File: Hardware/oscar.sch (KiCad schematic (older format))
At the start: 49 parts, among them J1 SWD_Header, J2 ChannelA_In, J3 ChannelB_In, J4 ChannelC_In, J5 ChA_Buff_Out, J6 ChB_Buff_Out, J7 ChC_Buff_Out, J8 MIDI_In, J9 Eurorack_16_pin_power, SW1 Left_Encoder, SW2 Right_Encoder, SW3 SW_Push, U1 STM32F446RETx, U2 ILI9341_SPI, U3 MCP6004, U4 TL074, U5 LM1117-3.3, Y1 Crystal

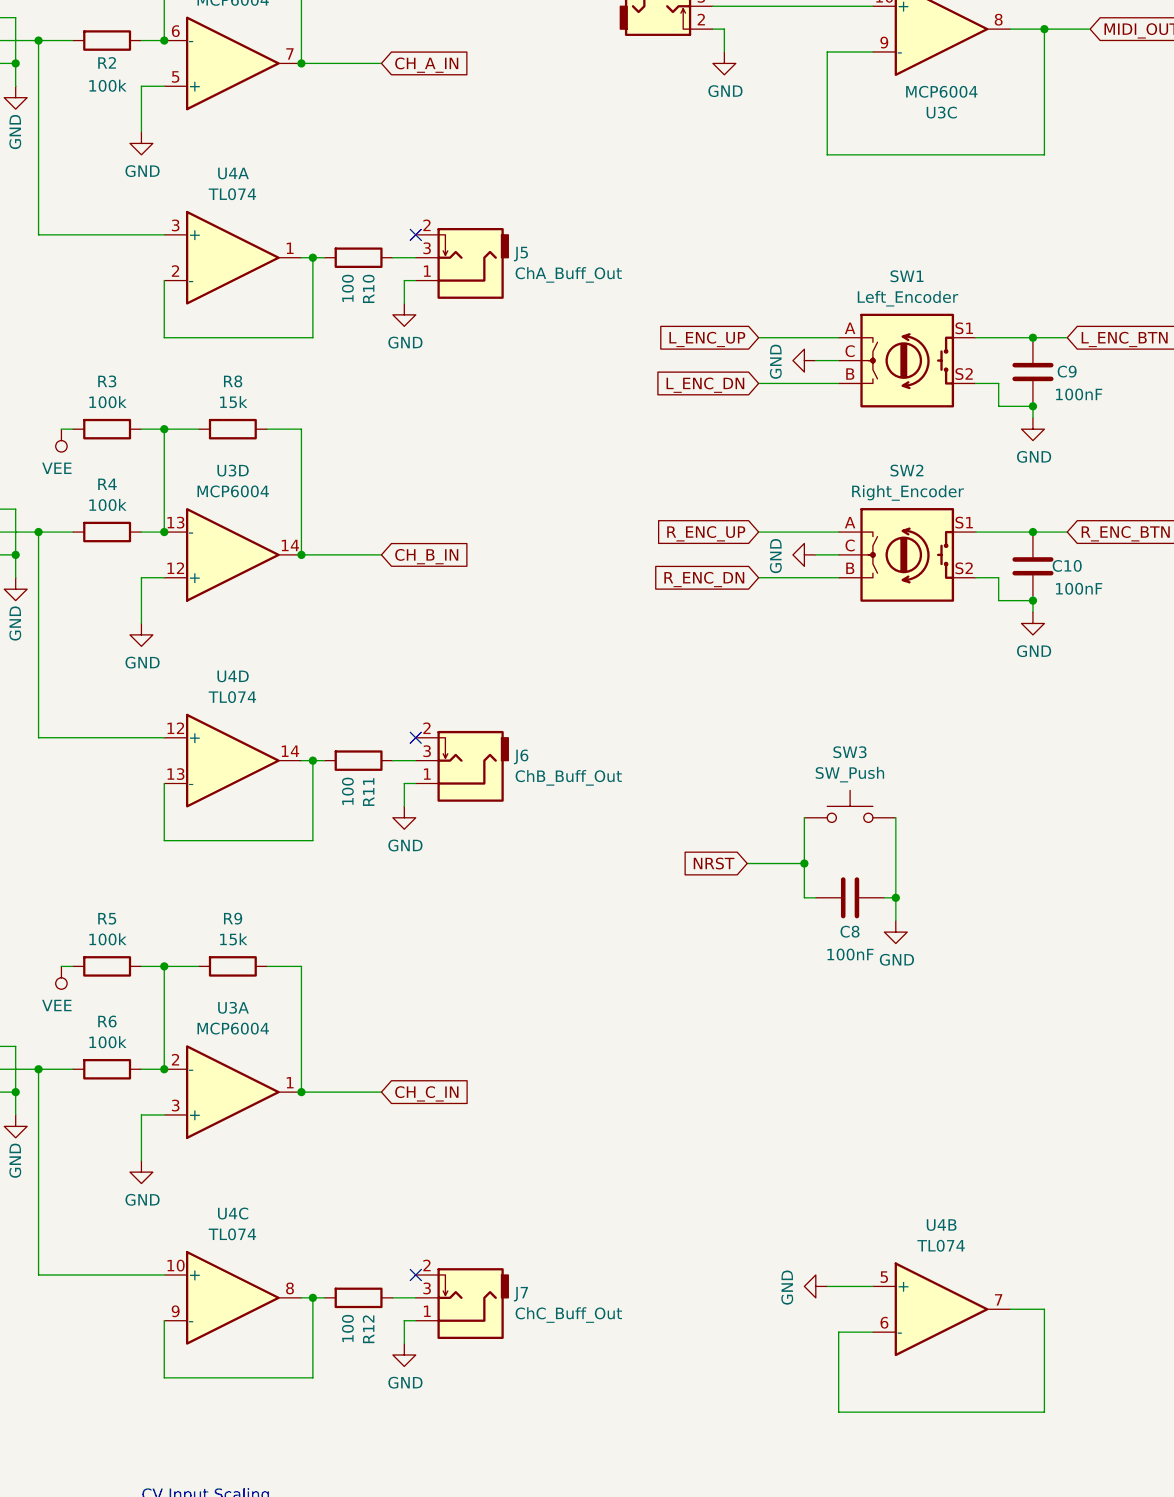
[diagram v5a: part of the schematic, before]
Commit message: MIDI uses ring buffer instead of queu and added clock
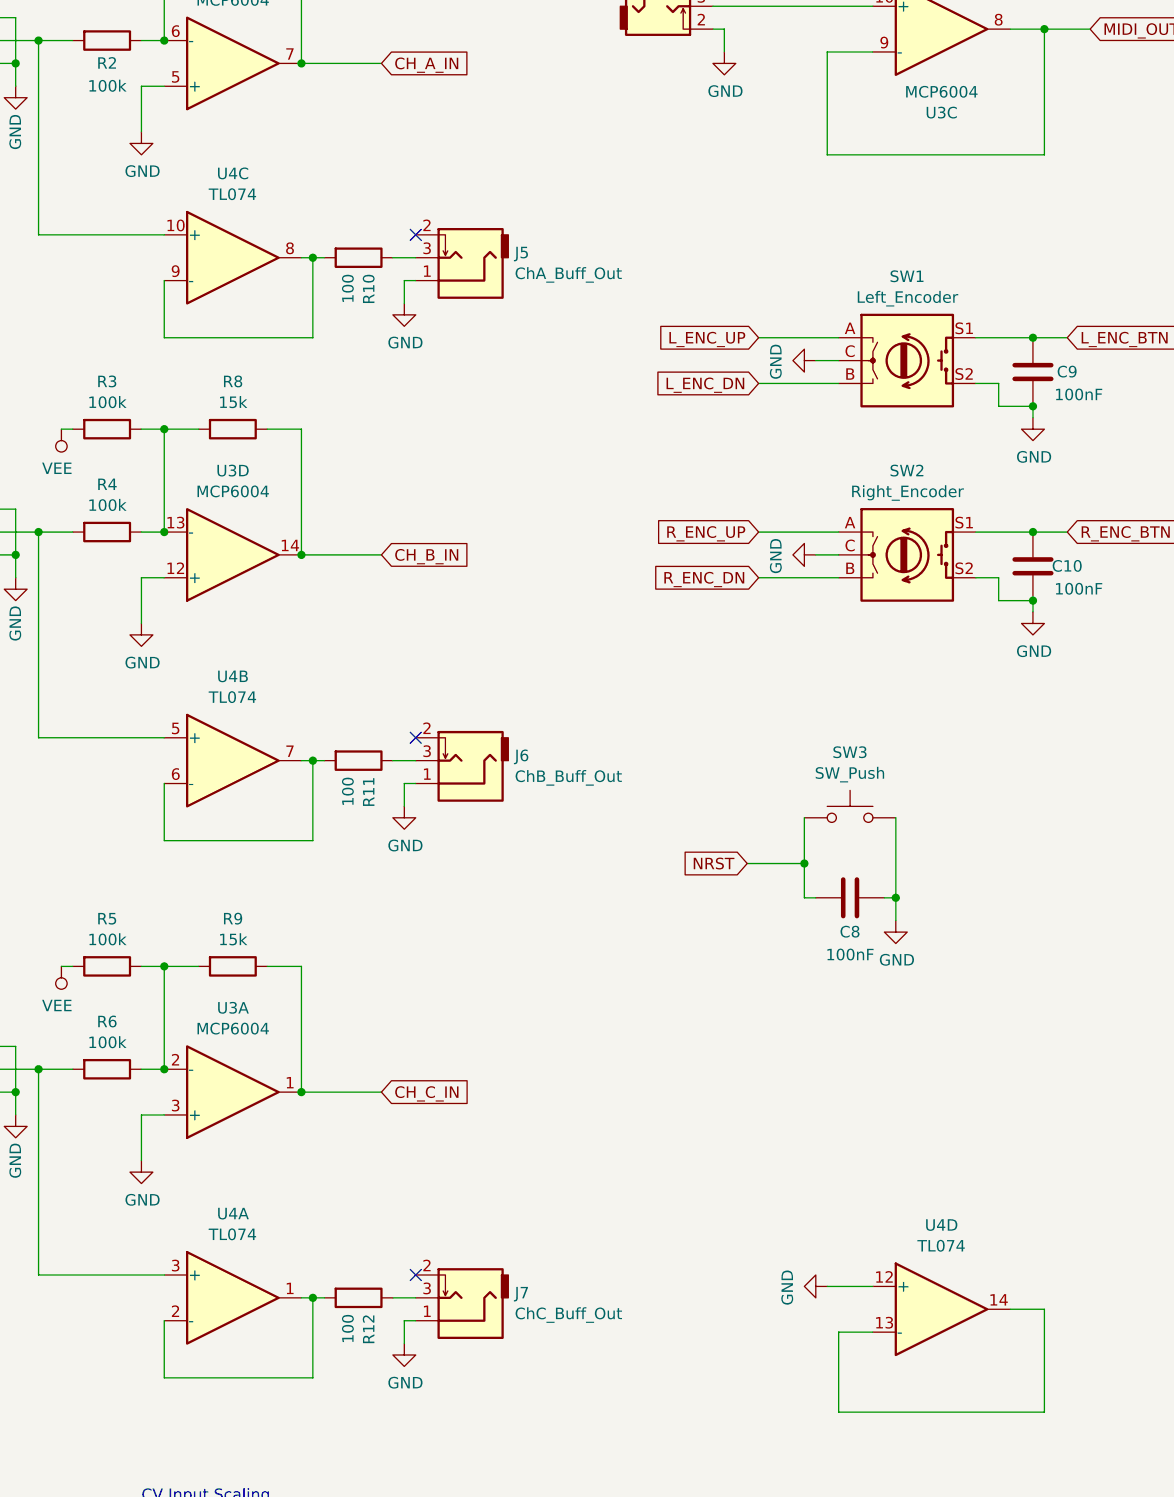
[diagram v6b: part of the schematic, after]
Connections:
- net GND: now also U4.12 (+); no longer U4.5 (+)
- net at J2.3, R2.2: now also U4.10 (+); no longer U4.3 (+)
- net at J3.3, R4.2: now also U4.5 (+); no longer U4.12 (+)
- net at J4.3, R6.2: now also U4.3 (+); no longer U4.10 (+)
- new net: R10.2, U4.8, U4.9 (-)
- new net: R11.2, U4.6 (-), U4.7
- new net: R12.2, U4.1, U4.2 (-)
- new net: U4.13 (-), U4.14
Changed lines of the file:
@@
 $Comp
 L Amplifier_Operational:TL074 U4
-U 1 1 5D2E5670
+U 3 1 5D2E5670
 P 6050 2400
 F 0 "U4" H 6050 2767 50  0000 C CNN
@@
 F 2 "SMD_Packages:SOIC-14_N" H 6000 2500 50  0001 C CNN
 F 3 "http://www.ti.com/lit/ds/symlink/tl071.pdf" H 6100 2600 50  0001 C CNN
-	1    6050 2400
+	3    6050 2400
 	1    0    0    -1
 $EndComp
 $Comp
 L Amplifier_Operational:TL074 U4
-U 4 1 5D2E8442
+U 2 1 5D2E8442
 P 6050 4600
 F 0 "U4" H 6050 4967 50  0000 C CNN
@@
 F 2 "SMD_Packages:SOIC-14_N" H 6000 4700 50  0001 C CNN
 F 3 "http://www.ti.com/lit/ds/symlink/tl071.pdf" H 6100 4800 50  0001 C CNN
-	4    6050 4600
+	2    6050 4600
 	1    0    0    -1
 $EndComp
 $Comp
 L Amplifier_Operational:TL074 U4
-U 3 1 5D2EA4AD
+U 1 1 5D2EA4AD
 P 6050 6950
 F 0 "U4" H 6050 7317 50  0000 C CNN
@@
 F 2 "SMD_Packages:SOIC-14_N" H 6000 7050 50  0001 C CNN
 F 3 "http://www.ti.com/lit/ds/symlink/tl071.pdf" H 6100 7150 50  0001 C CNN
-	3    6050 6950
+	1    6050 6950
 	1    0    0    -1
 $EndComp
 $Comp
 L Amplifier_Operational:TL074 U4
-U 2 1 5D2ECB47
+U 4 1 5D2ECB47
 P 9150 7000
 F 0 "U4" H 9150 7367 50  0000 C CNN
@@
 F 2 "SMD_Packages:SOIC-14_N" H 9100 7100 50  0001 C CNN
 F 3 "http://www.ti.com/lit/ds/symlink/tl071.pdf" H 9200 7200 50  0001 C CNN
-	2    9150 7000
+	4    9150 7000
 	1    0    0    -1
 $EndComp

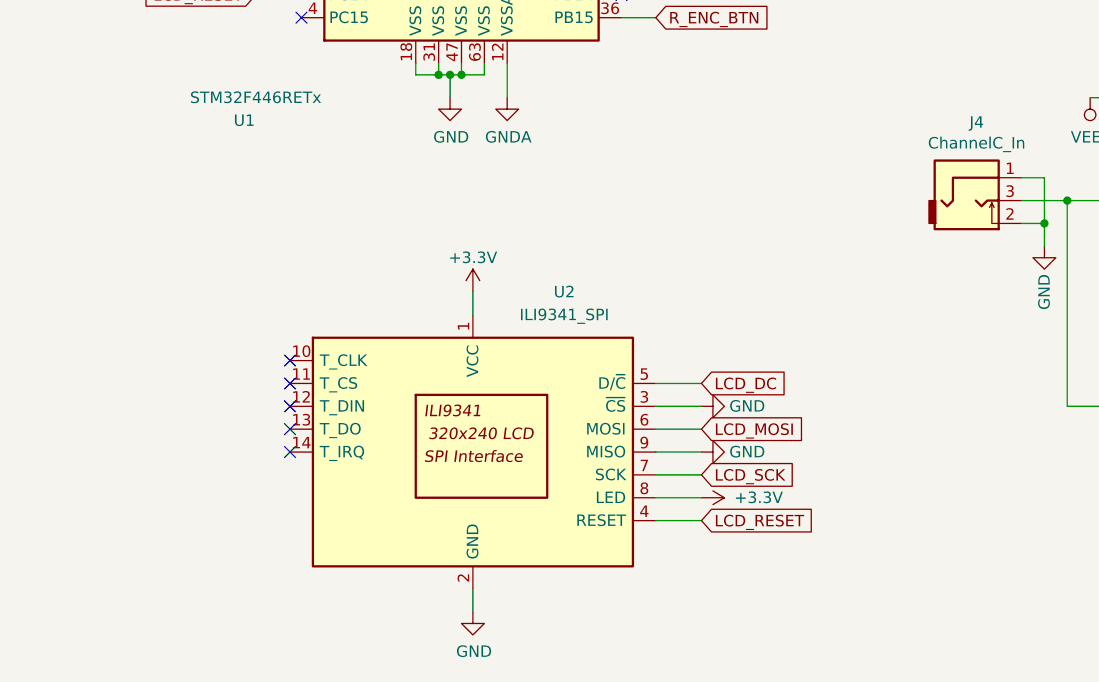
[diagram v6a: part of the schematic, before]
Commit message: Added LCD Solder pads
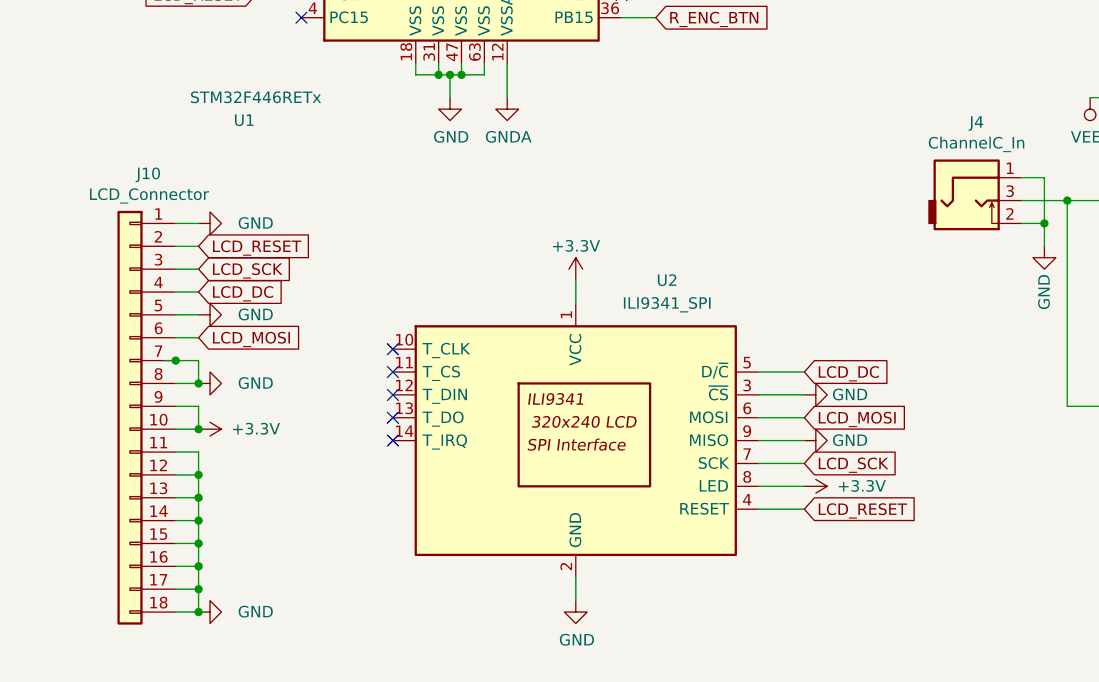
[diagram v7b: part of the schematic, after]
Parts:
- added J10: LCD_Connector, Custom_Footprints:18x0.8mmLCDConnector, symbol Connector_Generic:Conn_01x18
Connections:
- net +3V3: now also J10.10 (Pin_10), J10.9 (Pin_9)
- net GND: now also J10.1 (Pin_1), J10.11 (Pin_11), J10.12 (Pin_12), J10.13 (Pin_13), J10.14 (Pin_14), J10.15 (Pin_15), J10.16 (Pin_16), J10.17 (Pin_17), J10.18 (Pin_18), J10.5 (Pin_5), J10.7 (Pin_7), J10.8 (Pin_8)
- net LCD_DC: now also J10.4 (Pin_4)
- net LCD_MOSI: now also J10.6 (Pin_6)
- net LCD_RESET: now also J10.2 (Pin_2)
- net LCD_SCK: now also J10.3 (Pin_3)
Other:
- moved on the sheet: U2

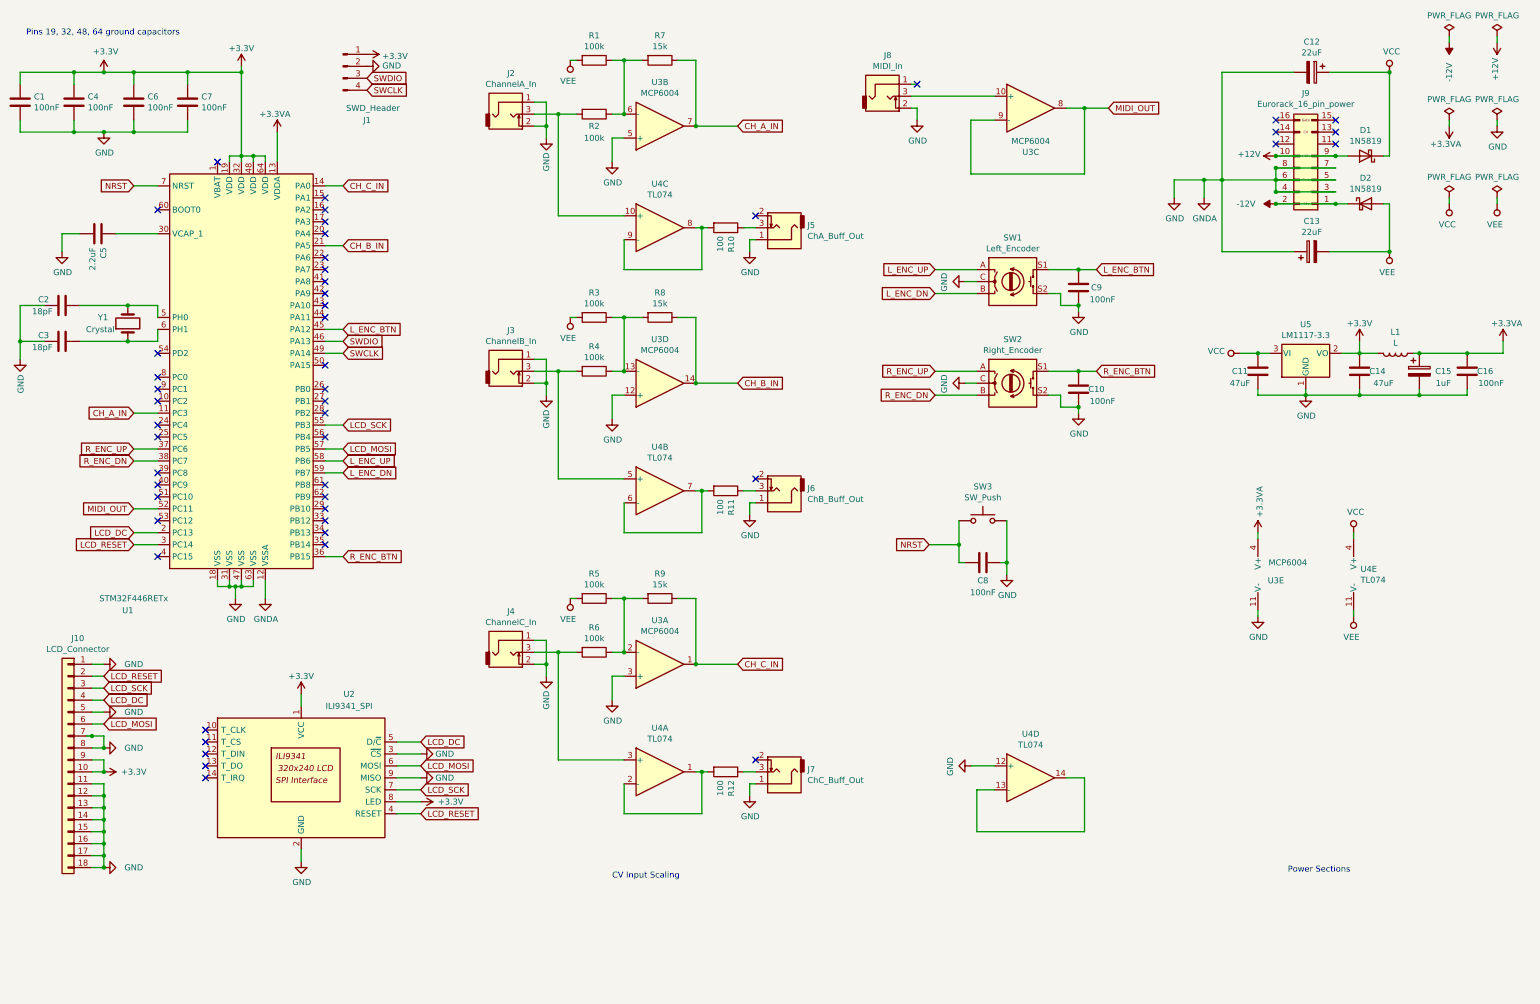
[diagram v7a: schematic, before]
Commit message: v1 PCB; added zero crossing count config to Circular mode; refactored variables into objects
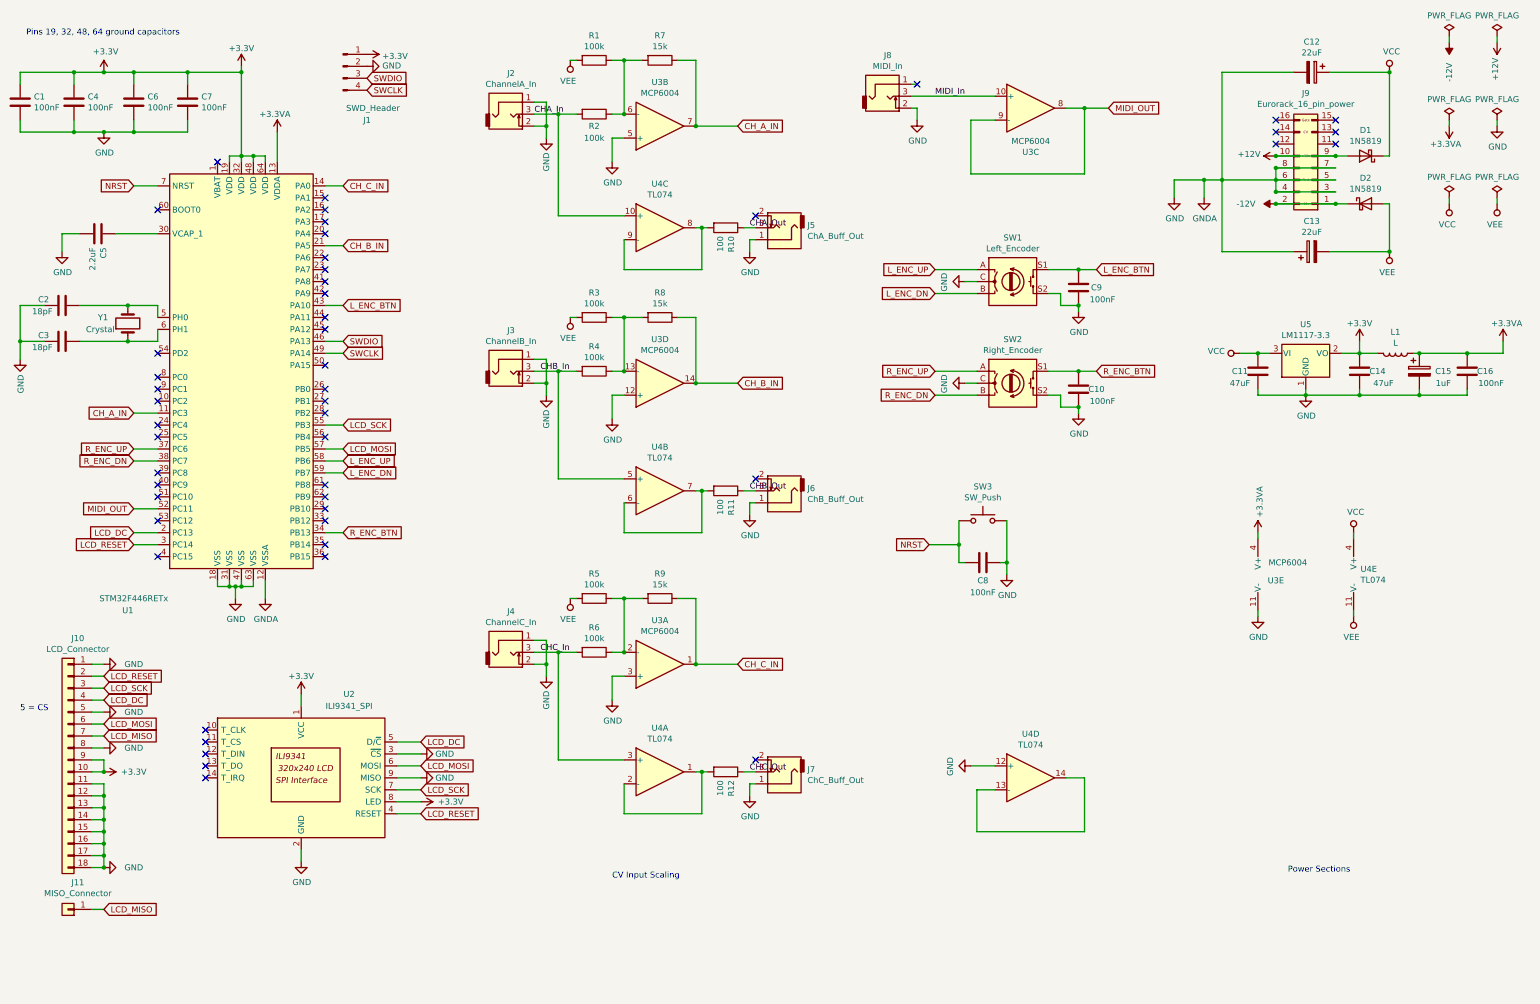
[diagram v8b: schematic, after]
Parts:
- added J11: MISO_Connector, Wire_Pads:SolderWirePad_single_2mmDrill, symbol Connector_Generic:Conn_01x01
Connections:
- net GND: no longer J10.7 (Pin_7)
- net L_ENC_BTN: now also U1.43 (PA10); no longer U1.45 (PA12)
- net R_ENC_BTN: now also U1.34 (PB13); no longer U1.36 (PB15)
- net CHA_In: now reaches J2.3, R2.2, U4.10 (+)
- net CHB_In: now reaches J3.3, R4.2, U4.5 (+)
- net CHC_In: now reaches J4.3, R6.2, U4.3 (+)
- net MIDI_In: now reaches J8.3, U3.10 (+)
- net CHA_Out: now reaches J5.3, R10.1
- net CHB_Out: now reaches J6.3, R11.1
- net CHC_Out: now reaches J7.3, R12.1
- new net LCD_MISO: J10.7 (Pin_7), J11.1 (Pin_1)
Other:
- note added: "5 = CS"
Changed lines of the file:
@@
 Text GLabel 3400 2050 2    50   Input ~ 0
 CH_C_IN
-Text GLabel 3400 3250 2    50   Input ~ 0
+Text GLabel 3400 3050 2    50   Input ~ 0
 L_ENC_BTN
 Text GLabel 3400 4350 2    50   Input ~ 0
@@
 Text GLabel 3400 4450 2    50   Input ~ 0
 L_ENC_DN
-Text GLabel 3400 5150 2    50   Input ~ 0
+Text GLabel 3400 4950 2    50   Input ~ 0
 R_ENC_BTN
 Text GLabel 1650 4250 0    50   Input ~ 0
@@
 	3250 2550 3400 2550
 Wire Wire Line
-	3400 5150 3250 5150
+	3400 4950 3250 4950
 Wire Wire Line
 	1850 5050 1650 5050
@@
 Wire Wire Line
 	1650 2050 1850 2050
-Wire Wire Line
-	3400 3250 3250 3250
 NoConn ~ 1850 3450
 NoConn ~ 1850 3750
@@
 NoConn ~ 1850 4850
 NoConn ~ 1850 3650
-NoConn ~ 3250 4950
+NoConn ~ 3250 5150
 NoConn ~ 3250 4850
 NoConn ~ 3250 4750
@@
 NoConn ~ 3250 4150
 NoConn ~ 3250 3150
-NoConn ~ 3250 3050
 NoConn ~ 3250 2950
 NoConn ~ 3250 2850
@@
 Text GLabel 1400 6350 2    50   Input ~ 0
 LCD_DC
-$Comp
-L power:GND #PWR0108
-U 1 1 5D43652F
-P 1400 6450
-F 0 "#PWR0108" H 1400 6200 50  0001 C CNN
-F 1 "GND" V 1400 6200 50  0000 C CNN
-F 2 "" H 1400 6450 50  0001 C CNN
-F 3 "" H 1400 6450 50  0001 C CNN
-	1    1400 6450
-	0    -1   -1   0
-$EndComp
 Wire Wire Line
 	1400 7350 1400 7450
@@
 LCD_MOSI
 Wire Wire Line
-	1250 6650 1300 6650
-Wire Wire Line
-	1400 6650 1400 6750
-Connection ~ 1300 6650
-Wire Wire Line
-	1300 6650 1400 6650
-Connection ~ 1400 6750
-Wire Wire Line
 	1300 6550 1400 6550
+Text GLabel 1400 6650 2    50   Input ~ 0
+LCD_MISO
+Text GLabel 1400 8100 2    50   Input ~ 0
+LCD_MISO
+$Comp
+L Connector_Generic:Conn_01x01 J11
+U 1 1 5D3E0C63
+P 1100 8100
+F 0 "J11" H 1018 7875 50  0000 C CNN
+F 1 "MISO_Connector" H 1018 7966 50  0000 C CNN
+F 2 "Wire_Pads:SolderWirePad_single_2mmDrill" H 1100 8100 50  0001 C CNN
+F 3 "~" H 1100 8100 50  0001 C CNN
+	1    1100 8100
+	-1   0    0    1
+$EndComp
+Wire Wire Line
+	1300 8100 1400 8100
+Text Label 5000 1450 0    50   ~ 0
+CHA_In
+Text Label 5050 3600 0    50   ~ 0
+CHB_In
+Text Label 5050 5950 0    50   ~ 0
+CHC_In
+Text Label 6800 6950 0    50   ~ 0
+CHC_Out
+Text Label 6800 4600 0    50   ~ 0
+CHB_Out
+Text Label 6800 2400 0    50   ~ 0
+CHA_Out
+Text Label 8350 1300 0    50   ~ 0
+MIDI_In
+Wire Wire Line
+	1400 6650 1300 6650
+$Comp
+L power:GND #PWR0108
+U 1 1 5D4C4EDD
+P 1400 6450
+F 0 "#PWR0108" H 1400 6200 50  0001 C CNN
+F 1 "GND" V 1400 6200 50  0000 C CNN
+F 2 "" H 1400 6450 50  0001 C CNN
+F 3 "" H 1400 6450 50  0001 C CNN
+	1    1400 6450
+	0    -1   -1   0
+$EndComp
+Text Notes 700  6450 0    50   ~ 0
+5 = CS
+Wire Wire Line
+	3250 3050 3400 3050
+NoConn ~ 3250 3250
 $EndSCHEMATC
